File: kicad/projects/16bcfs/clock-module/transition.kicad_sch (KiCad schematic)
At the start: 3 parts, among them U3 74HC32, U4 74HC74, U6 74HC08

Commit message: Clean up the Reset and Clock Modules
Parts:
- added U10: 74HC08, symbol eryjus:74HC08
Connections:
- net VCC: now also U4.4 (~{S}); no longer U4.1 (~{R})
- net ~{CPYHLD}: now also U4.1 (~{R}); no longer U4.4 (~{S})
- net at U4.5 (Q): now also U10.1; no longer U3.4
- new net: U10.3, U3.4
- new net ~{StepSel}: U10.2
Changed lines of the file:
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@@
     (comment 1 "Adam Clark (@eryjus)")
   )
-  (wire (pts (xy 130.81 63.5) (xy 163.83 63.5))
-    (stroke (width 0) (type default))
-  )
-  (wire (pts (xy 163.83 83.82) (xy 184.15 83.82))
+  (wire (pts (xy 173.99 66.04) (xy 175.26 66.04))
+    (stroke (width 0) (type default))
+  )
+  (wire (pts (xy 130.81 63.5) (xy 158.75 63.5))
+    (stroke (width 0) (type default))
+  )
+  (wire (pts (xy 123.19 50.8) (xy 123.19 58.42))
+    (stroke (width 0) (type default))
+  )
+  (wire (pts (xy 156.21 68.58) (xy 158.75 68.58))
+    (stroke (width 0) (type default))
+  )
+  (wire (pts (xy 175.26 83.82) (xy 184.15 83.82))
     (stroke (width 0) (type default))
   )
@@
     (stroke (width 0) (type default))
   )
-  (wire (pts (xy 123.19 73.66) (xy 123.19 77.47))
-    (stroke (width 0) (type default))
-  )
-  (wire (pts (xy 123.19 52.07) (xy 123.19 58.42))
-    (stroke (width 0) (type default))
-  )
   (wire (pts (xy 163.83 88.9) (xy 184.15 88.9))
     (stroke (width 0) (type default))
@@
     (stroke (width 0) (type default))
   )
-  (wire (pts (xy 123.19 77.47) (xy 142.24 77.47))
-    (stroke (width 0) (type default))
-  )
   (wire (pts (xy 71.12 76.2) (xy 78.74 76.2))
     (stroke (width 0) (type default))
@@
     (stroke (width 0) (type default))
   )
+  (wire (pts (xy 123.19 73.66) (xy 123.19 76.2))
+    (stroke (width 0) (type default))
+  )
   (wire (pts (xy 110.49 63.5) (xy 115.57 63.5))
     (stroke (width 0) (type default))
   )
+  (wire (pts (xy 123.19 76.2) (xy 121.92 76.2))
+    (stroke (width 0) (type default))
+  )
   (wire (pts (xy 55.88 91.44) (xy 46.99 91.44))
     (stroke (width 0) (type default))
@@
     (stroke (width 0) (type default))
   )
-  (wire (pts (xy 163.83 63.5) (xy 163.83 83.82))
+  (wire (pts (xy 175.26 66.04) (xy 175.26 83.82))
     (stroke (width 0) (type default))
   )
@@
   )
   (wire (pts (xy 78.74 68.58) (xy 83.82 68.58))
-    (stroke (width 0) (type default))
-  )
-  (wire (pts (xy 107.95 52.07) (xy 123.19 52.07))
-    (stroke (width 0) (type default))
-  )
-  (wire (pts (xy 142.24 77.47) (xy 142.24 35.56))
     (stroke (width 0) (type default))
   )
@@
     (effects (font (size 1.27 1.27)) (justify right))
   )
+  (hierarchical_label "~{StepSel}" (shape input) (at 156.21 68.58 180) (fields_autoplaced)
+    (effects (font (size 1.27 1.27)) (justify right))
+  )
   (hierarchical_label "Step_Sel" (shape input) (at 46.99 96.52 180) (fields_autoplaced)
     (effects (font (size 1.27 1.27)) (justify right))
@@
     (effects (font (size 1.27 1.27)) (justify right))
   )
-  (hierarchical_label "~{CPYHLD}" (shape input) (at 107.95 52.07 180) (fields_autoplaced)
+  (hierarchical_label "~{CPYHLD}" (shape input) (at 121.92 76.2 180) (fields_autoplaced)
     (effects (font (size 1.27 1.27)) (justify right))
   )
@@
     )
   )
-  (symbol (lib_id "power:VCC") (at 142.24 35.56 0) (unit 1)
+  (symbol (lib_id "power:VCC") (at 123.19 50.8 0) (unit 1)
     (in_bom yes) (on_board yes) (dnp no) (fields_autoplaced)
-    (property "Reference" "#PWR013" (at 142.24 39.37 0)
-      (effects (font (size 1.27 1.27)) hide)
-    )
-    (property "Value" "VCC" (at 142.24 30.48 0)
+    (property "Reference" "#PWR013" (at 123.19 54.61 0)
+      (effects (font (size 1.27 1.27)) hide)
+    )
+    (property "Value" "VCC" (at 123.19 45.72 0)
       (effects (font (size 1.27 1.27)))
     )
-    (property "Footprint" "" (at 142.24 35.56 0)
-      (effects (font (size 1.27 1.27)) hide)
-    )
-    (property "Datasheet" "" (at 142.24 35.56 0)
+    (property "Footprint" "" (at 123.19 50.8 0)
+      (effects (font (size 1.27 1.27)) hide)
+    )
+    (property "Datasheet" "" (at 123.19 50.8 0)
       (effects (font (size 1.27 1.27)) hide)
     )
@@
         )
       )
+    )
+  )
+  (symbol (lib_id "eryjus:74HC08") (at 166.37 66.04 0) (unit 1)
+    (in_bom yes) (on_board yes) (dnp no)
+    (property "Reference" "U10" (at 162.56 63.5 0)
+      (effects (font (size 1.27 1.27)) (justify left))
+    )
+    (property "Value" "74HC08" (at 162.56 66.04 0)
+      (effects (font (size 1.27 1.27)) (justify left))
+    )
+    (property "Footprint" "" (at 166.37 66.04 0)
+      (effects (font (size 1.27 1.27)) hide)
+    )
+    (property "Datasheet" "http://www.ti.com/lit/gpn/sn74HC08" (at 166.37 66.04 0)
+      (effects (font (size 1.27 1.27)) hide)
+    )
+    (pin "2")
+    (pin "14")
+    (pin "7")
+    (pin "1")
+    (pin "4")
+    (pin "8")
+    (pin "13")
+    (pin "12")
+    (pin "11")
+    (pin "6")
+    (pin "9")
+    (pin "10")
+    (pin "5")
+    (pin "3")
+    (instances
+      (project "clock-module"
+        (path "/d0ae44e5-d74e-4df6-bf3d-e0535c5a7785/a6ceb695-9aed-4445-8c30-2b58b21d3a82"
+          (reference "U10") (unit 1)
+        )
+      )

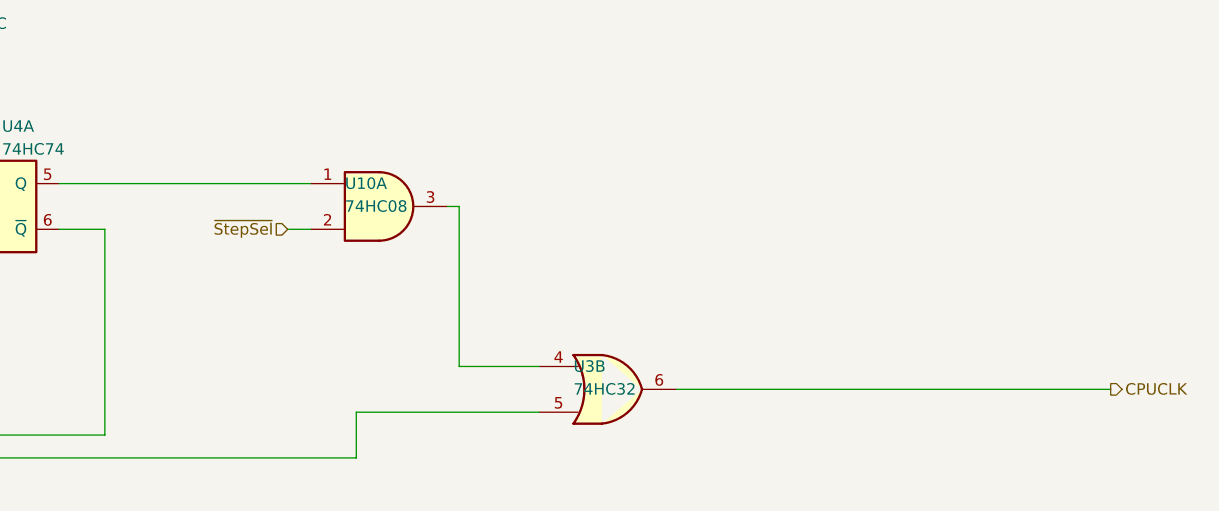
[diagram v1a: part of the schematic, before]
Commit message: Schematic changes for clock and control ROM
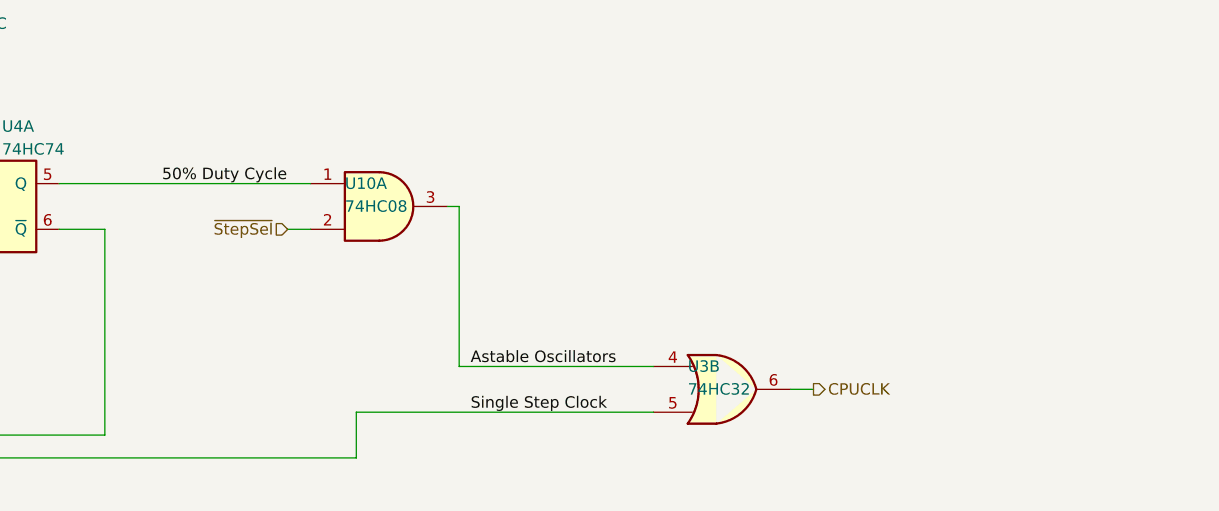
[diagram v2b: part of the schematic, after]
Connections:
- net Single Step Clock: now reaches U3.5, U6.11
- net 50% Duty Cycle: now reaches U10.1, U4.5 (Q)
- net Astable Oscillators: now reaches U10.3, U3.4
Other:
- moved on the sheet: U3B
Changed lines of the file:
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@@
     (stroke (width 0) (type default))
   )
-  (wire (pts (xy 175.26 83.82) (xy 184.15 83.82))
+  (wire (pts (xy 175.26 83.82) (xy 196.85 83.82))
     (stroke (width 0) (type default))
   )
@@
     (stroke (width 0) (type default))
   )
-  (wire (pts (xy 163.83 88.9) (xy 184.15 88.9))
+  (wire (pts (xy 163.83 88.9) (xy 196.85 88.9))
     (stroke (width 0) (type default))
   )
@@
     (stroke (width 0) (type default))
   )
-  (wire (pts (xy 199.39 86.36) (xy 247.65 86.36))
+  (wire (pts (xy 212.09 86.36) (xy 214.63 86.36))
     (stroke (width 0) (type default))
   )
@@
     (stroke (width 0) (type default))
   )
+  (label "50% Duty Cycle" (at 142.24 63.5 0) (fields_autoplaced)
+    (effects (font (size 1.27 1.27)) (justify left bottom))
+  )
+  (label "Astable Oscillators" (at 176.53 83.82 0) (fields_autoplaced)
+    (effects (font (size 1.27 1.27)) (justify left bottom))
+  )
+  (label "Single Step Clock" (at 176.53 88.9 0) (fields_autoplaced)
+    (effects (font (size 1.27 1.27)) (justify left bottom))
+  )
   (hierarchical_label "Adjustable Clock" (shape input) (at 46.99 73.66 180) (fields_autoplaced)
     (effects (font (size 1.27 1.27)) (justify right))
@@
     (effects (font (size 1.27 1.27)) (justify right))
   )
-  (hierarchical_label "CPUCLK" (shape output) (at 247.65 86.36 0) (fields_autoplaced)
+  (hierarchical_label "CPUCLK" (shape output) (at 214.63 86.36 0) (fields_autoplaced)
     (effects (font (size 1.27 1.27)) (justify left))
   )
@@
     )
   )
-  (symbol (lib_id "eryjus:74HC32") (at 191.77 86.36 0) (unit 2)
-    (in_bom yes) (on_board yes) (dnp no)
-    (property "Reference" "U3" (at 187.96 83.82 0)
-      (effects (font (size 1.27 1.27)) (justify left))
-    )
-    (property "Value" "74HC32" (at 187.96 86.36 0)
-      (effects (font (size 1.27 1.27)) (justify left))
-    )
-    (property "Footprint" "" (at 191.77 86.36 0)
-      (effects (font (size 1.27 1.27)) hide)
-    )
-    (property "Datasheet" "http://www.ti.com/lit/gpn/sn74HC32" (at 191.77 86.36 0)
-      (effects (font (size 1.27 1.27)) hide)
-    )
+  (symbol (lib_id "eryjus:74HC32") (at 204.47 86.36 0) (unit 2)
+    (in_bom yes) (on_board yes) (dnp no)
+    (property "Reference" "U3" (at 200.66 83.82 0)
+      (effects (font (size 1.27 1.27)) (justify left))
+    )
+    (property "Value" "74HC32" (at 200.66 86.36 0)
+      (effects (font (size 1.27 1.27)) (justify left))
+    )
+    (property "Footprint" "" (at 204.47 86.36 0)
+      (effects (font (size 1.27 1.27)) hide)
+    )
+    (property "Datasheet" "http://www.ti.com/lit/gpn/sn74HC32" (at 204.47 86.36 0)
+      (effects (font (size 1.27 1.27)) hide)
+    )
